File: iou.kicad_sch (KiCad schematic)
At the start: 46 parts, among them Q2 DMG1012TQ-7, U1 LSF0108BQ-Q100X, U2 MIC5504-3.3YM5-TR, U3 LSF0102DDFR, U4 MIC5365-1.2YC5-TR, U5 74LVC245ABQ,115, U6 ICE5LP1K-SG48ITR, U7 W25X20CLUXIG_TR

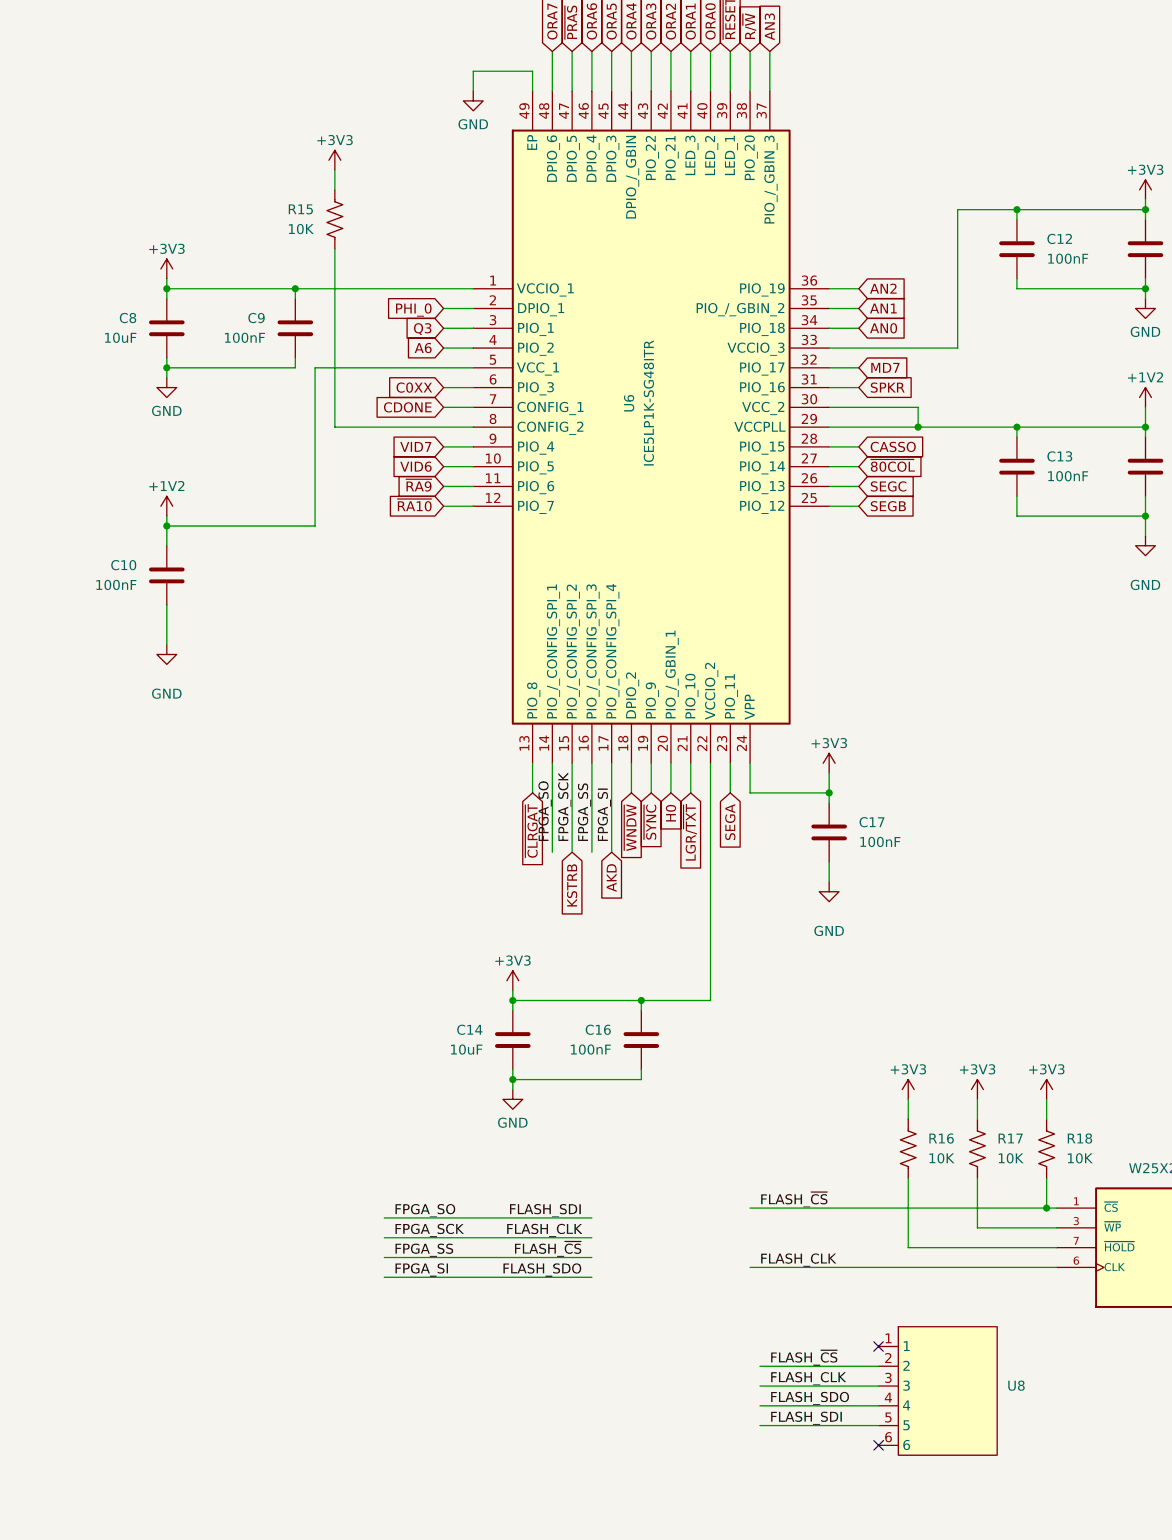
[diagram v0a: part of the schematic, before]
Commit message: Changed the connector to TC2050
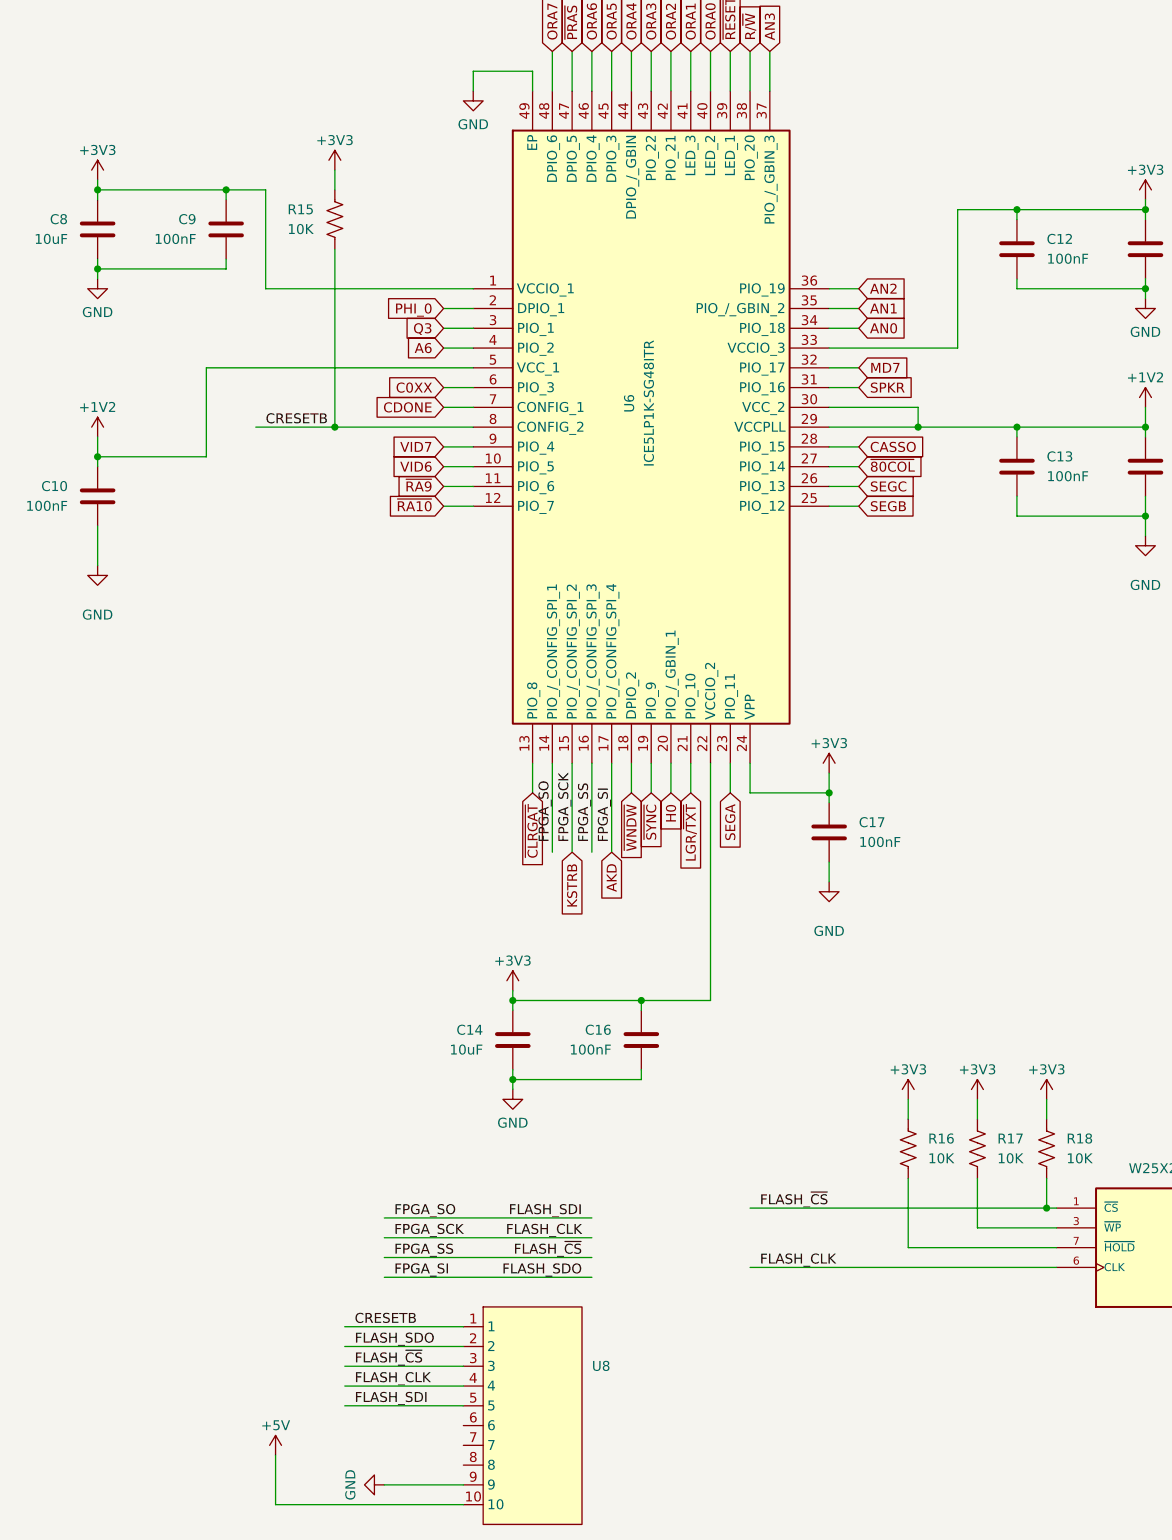
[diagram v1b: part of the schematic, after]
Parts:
- U8: footprint Connector:Tag-Connect_TC2030-IDC-NL_2x03_P1.27mm_Vertical -> 000_Footprints:Tag-Connect_TC2050-IDC-NL_2x05_P1.27mm_Vertical
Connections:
- net +5V: now also U8.10
- net AKD: now also U8.2; no longer U8.4
- net FLASH_~{CS}: now also U8.3; no longer U8.2
- net GND: now also U8.9
- net KSTRB: now also U8.4; no longer U8.3
- net CRESETB: now reaches U8.1
- net CRESETB: now also R15.2, U6.8 (CONFIG_2)
- no-connect marks 3 -> 1
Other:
- moved on the sheet: C10, C8, C9
